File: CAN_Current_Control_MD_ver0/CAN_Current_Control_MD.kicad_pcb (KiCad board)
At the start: 2 copper layers, 75 x 81 mm, 200 parts, among them J1 SWD, J10 FAN, J11 OUT_0, J12 OUT_1, J13 VALVE, J2 CAN, J3 CAN, J4 ENC0, J5 ENC1, J6 I/O_0, J7 I/O_1, J8 BATT_IN, J9 BATT_IN, Q1 MOSFET_N, Q10 NPN, Q2 MOSFET_N, Q3 MOSFET_N, Q4 MOSFET_N, Q5 MOSFET_N, Q6 MOSFET_N, Q7 MOSFET_N, Q8 MOSFET_N, Q9 NPN, SW1 SW0, SW2 SW1, SW3 RST, U1 BD33FA1, U10 NCP5104, U11 NCP5104, U12 BD9G101G, U13 INA181A1, U14 INA181A1, U15 LOGO, U2 ISO1050DUB, U3 STM32F405RG, U4 ADRESS, U5 AZ1086H, U6 BD9G101G, U7 AQM0802, U8 NCP5104, U9 NCP5104, Y1 8MHz

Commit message: 電流制御MD(仮)配線(仮)完成(仮)
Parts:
- moved R31 0.39 mm to (186.5, 122.3)
- moved C14 0.28 mm to (188.3, 122.2)
- moved R30 0.25 mm to (191.2, 129.5)
- moved R32 0.25 mm to (189.8, 129.5)
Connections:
- U3 pad 20: /Substrate_Temp -> /ADRESS_1
- U3 pad 21: /ADRESS_4 -> /Substrate_Temp
- U3 pad 23: /ADRESS_1 -> /ADRESS_4
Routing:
- net GNDPWR: track 84.2 -> 164.3 mm, vias 93 -> 115
- net /ADRESS_1: track 0.00 -> 45.3 mm, vias 0 -> 4
- net /ADRESS_4: track 0.00 -> 38.4 mm, vias 0 -> 4
- net /ADRESS_8: track 0.00 -> 31.5 mm, vias 0 -> 6
- net /SWDIO: track 40.3 -> 45.4 mm
- net +5VP: track 113.0 -> 116.7 mm
- net /ADRESS_2: track 36.5 -> 38.6 mm
- net /SWCLK: track 41.3 -> 43.0 mm
- net Net-(C14-Pad1): track 3.17 -> 1.46 mm
- net /I2C2_SCL: track 10.7 -> 12.2 mm
- net /I2C2_SDA: track 8.92 -> 10.4 mm
- net /TIM3_CH2: track 39.1 -> 40.3 mm
- net /MD1R_Temp: track 49.1 -> 49.9 mm
- net /TIM3_CH1: track 41.5 -> 42.1 mm
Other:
- board text added: "12VP"
- board text added: "3V3"
- board text added: "CLK"
- board text added: "DIO"
- board text added: "Designed by A.Mizuta in 2020/03/01."
- board text added: "~RST"
- board text removed: "Designed by A.Mizuta in 2020/03/0."

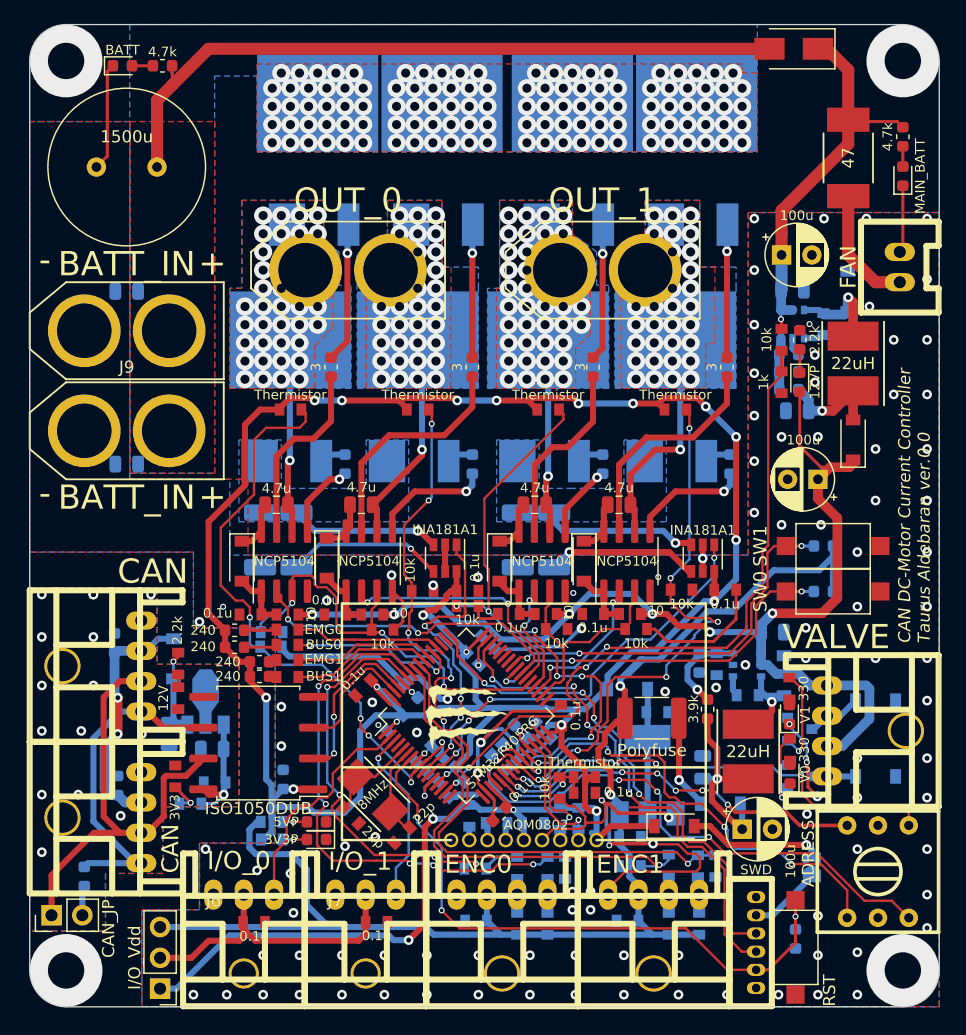
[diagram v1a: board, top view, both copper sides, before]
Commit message: 電流制御MDシリアル通信ポート忘れていたので，追加した
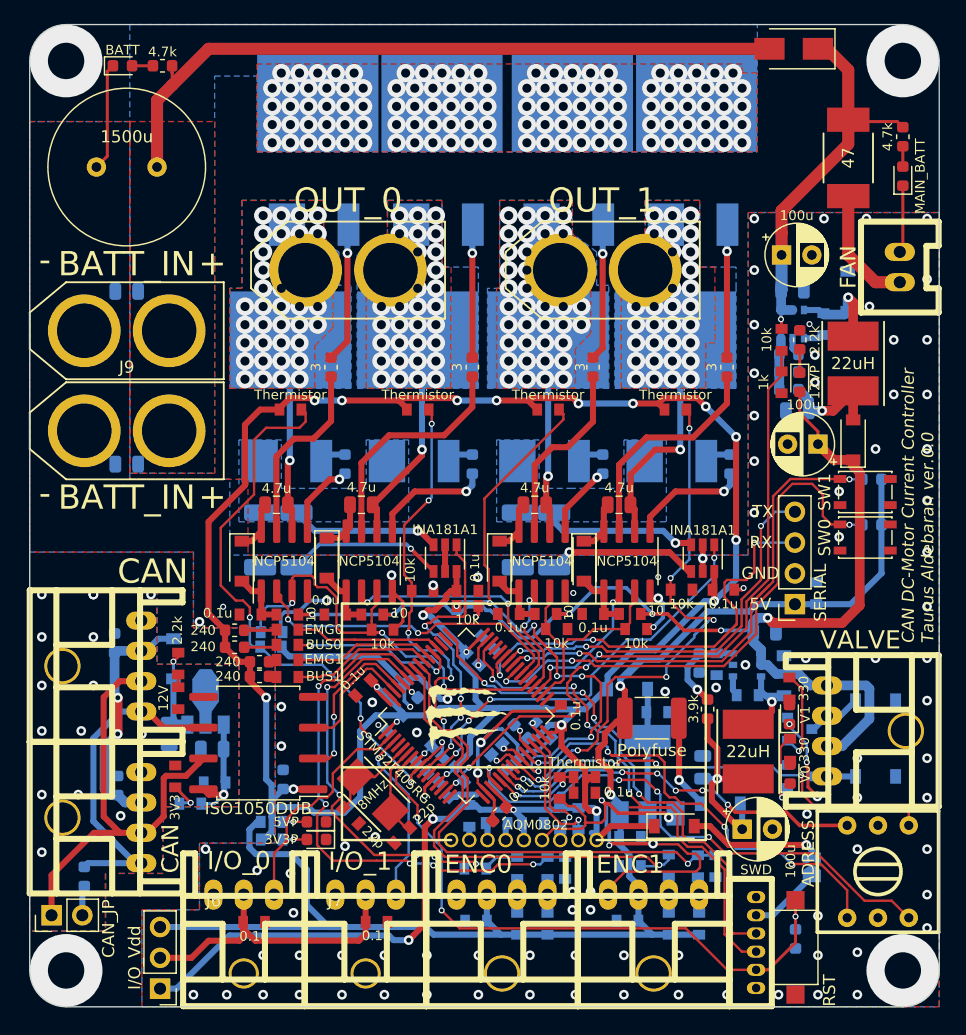
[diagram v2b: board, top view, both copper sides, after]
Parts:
- added C57: 0.1u, Mizz_lib:1608_WP, B.Cu at (210.9, 110.9)
- added J14: SERIAL, Connector_PinSocket_2.54mm:PinSocket_1x04_P2.54mm_Vertical, F.Cu at (209.1, 111.8)
- SW1, SW2: footprint Button_Switch_SMD:SW_SPST_CK_RS282G05A3 -> Button_Switch_SMD:SW_SPST_PTS810
- moved R10 6.80 mm to (215.4, 101.5)
- moved R8 6.80 mm to (215.4, 105.2)
- moved SW1 5.18 mm to (214.9, 106.3)
- moved SW2 5.18 mm to (214.9, 102.5)
- moved C50 2.90 mm to (211.0, 98.6)
- moved C25 0.65 mm to (206.6, 114.1)
- moved C56 0.15 mm to (203.2, 110.6)
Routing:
- net /USART1_RX: track 0.00 -> 38.4 mm, vias 0 -> 3
- net /USART1_TX: track 0.00 -> 33.0 mm, vias 0 -> 3
- net /SW0: track 31.2 -> 45.8 mm
- net /SW1: track 32.0 -> 43.4 mm
- net GNDPWR: track 164.3 -> 155.9 mm, vias 115 -> 113
- net +5VP: track 116.7 -> 124.0 mm
- net /MD1L_Temp: track 53.2 -> 56.0 mm
- net +12P: track 94.5 -> 96.9 mm
- net /MD1R_Temp: track 49.9 -> 51.2 mm
- net /EN0: track 36.8 -> 37.3 mm
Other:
- board text added: "5V"
- board text added: "H"
- board text added: "L"
- board text added: "RX"
- board text added: "TX"

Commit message: いろいろ修正しました
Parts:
- R50, R51, R52, R53, R54, R55, R56, R57: value 3 -> FILTER
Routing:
- net GNDPWR: track 155.9 -> 157.1 mm
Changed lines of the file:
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@@
     (thickness 1.6)
     (drawings 49)
-    (tracks 2194)
+    (tracks 2195)
     (zones 0)
     (modules 202)
@@
   )
   (setup
-    (last_trace_width 0.3)
+    (last_trace_width 0.25)
     (user_trace_width 0.2)
     (user_trace_width 0.3)
@@
       (effects (font (size 1 1) (thickness 0.15)))
     )
-    (fp_text value 3 (at 0 1.25 90) (layer F.SilkS)
+    (fp_text value FILTER (at 0 1.25 90) (layer F.SilkS)
       (effects (font (size 0.8 0.8) (thickness 0.15)))
     )
@@
       (effects (font (size 1 1) (thickness 0.15)) (justify mirror))
     )
-    (fp_text value 3 (at 0 -1.25 90) (layer B.SilkS)
+    (fp_text value FILTER (at 0 -1.25 90) (layer B.SilkS)
       (effects (font (size 0.8 0.8) (thickness 0.15)) (justify mirror))
     )
@@
       (effects (font (size 1 1) (thickness 0.15)))
     )
-    (fp_text value 3 (at 0 1.25 90) (layer F.SilkS)
+    (fp_text value FILTER (at 0 1.25 90) (layer F.SilkS)
       (effects (font (size 0.8 0.8) (thickness 0.15)))
     )
@@
       (effects (font (size 1 1) (thickness 0.15)) (justify mirror))
     )
-    (fp_text value 3 (at 0 -1.25 90) (layer B.SilkS)
+    (fp_text value FILTER (at 0 -1.25 90) (layer B.SilkS)
       (effects (font (size 0.8 0.8) (thickness 0.15)) (justify mirror))
     )
@@
       (effects (font (size 1 1) (thickness 0.15)))
     )
-    (fp_text value 3 (at 0 1.05 90) (layer F.SilkS)
+    (fp_text value FILTER (at 0 1.2 90) (layer F.SilkS)
       (effects (font (size 0.8 0.8) (thickness 0.15)))
     )
@@
       (effects (font (size 1 1) (thickness 0.15)) (justify mirror))
     )
-    (fp_text value 3 (at 0 -1.25 90) (layer B.SilkS)
+    (fp_text value FILTER (at 0 -1.25 90) (layer B.SilkS)
       (effects (font (size 0.8 0.8) (thickness 0.15)) (justify mirror))
     )
@@
       (effects (font (size 1 1) (thickness 0.15)))
     )
-    (fp_text value 3 (at 0 1.25 90) (layer F.SilkS)
+    (fp_text value FILTER (at 0 1.25 90) (layer F.SilkS)
       (effects (font (size 0.8 0.8) (thickness 0.15)))
     )
@@
       (effects (font (size 1 1) (thickness 0.15)) (justify mirror))
     )
-    (fp_text value 3 (at 0 -1.25 90) (layer B.SilkS)
+    (fp_text value FILTER (at 0 -1.25 90) (layer B.SilkS)
       (effects (font (size 0.8 0.8) (thickness 0.15)) (justify mirror))
     )
@@
   (via (at 160.5 132) (size 0.8) (drill 0.4) (layers F.Cu B.Cu) (net 5))
   (via (at 166.75 123.5) (size 0.8) (drill 0.4) (layers F.Cu B.Cu) (net 5))
-  (via (at 166.75 120.25) (size 0.8) (drill 0.4) (layers F.Cu B.Cu) (net 5))
   (via (at 160 113.25) (size 0.8) (drill 0.4) (layers F.Cu B.Cu) (net 5))
   (segment (start 208.9 90.7125) (end 209.3875 91.2) (width 0.5) (layer B.Cu) (net 5))
@@
   (segment (start 193.450001 129.509999) (end 193.450001 128.250001) (width 0.2) (layer F.Cu) (net 5))
   (segment (start 193.15 129.81) (end 193.450001 129.509999) (width 0.2) (layer F.Cu) (net 5))
-  (via (at 174.25 119.89) (size 0.8) (drill 0.4) (layers F.Cu B.Cu) (net 5))
   (via (at 174.75 121.76) (size 0.5) (drill 0.3) (layers F.Cu B.Cu) (net 5))
   (via (at 197.83 109.56) (size 0.5) (drill 0.3) (layers F.Cu B.Cu) (net 5))
@@
   (segment (start 183 111.95) (end 183 112.642501) (width 0.3) (layer F.Cu) (net 5))
   (segment (start 183 112.642501) (end 182.78 112.862501) (width 0.3) (layer F.Cu) (net 5))
+  (segment (start 169.5 117.5) (end 170.72217 117.5) (width 0.5) (layer B.Cu) (net 5))
+  (via (at 168.75 120.5) (size 0.8) (drill 0.4) (layers F.Cu B.Cu) (net 5))
+  (via (at 166.75 119) (size 0.8) (drill 0.4) (layers F.Cu B.Cu) (net 5))
   (segment (start 175.749569 127.435355) (end 175.75 127.434924) (width 0.2) (layer F.Cu) (net 6))
   (segment (start 175.749569 128.949569) (end 175.749569 127.435355) (width 0.2) (layer F.Cu) (net 6))
@@
   (segment (start 164.153882 112.06388) (end 164.153882 112.889669) (width 0.2) (layer F.Cu) (net 23))
   (segment (start 165.5 97.25) (end 164.5 98.25) (width 0.2) (layer F.Cu) (net 23))
-  (segment (start 165 115.3) (end 165.03 115.3) (width 0.2) (layer B.Cu) (net 23))
-  (segment (start 166.53 116.8) (end 170.124301 116.8) (width 0.2) (layer B.Cu) (net 23))
-  (segment (start 165.03 115.3) (end 166.53 116.8) (width 0.2) (layer B.Cu) (net 23))
   (via (at 173.290025 121.220025) (size 0.5) (drill 0.3) (layers F.Cu B.Cu) (net 23))
-  (segment (start 170.124301 116.8) (end 173.290025 119.965724) (width 0.2) (layer B.Cu) (net 23))
-  (segment (start 173.290025 119.965724) (end 173.290025 121.220025) (width 0.2) (layer B.Cu) (net 23))
   (via (at 173.95 122.63) (size 0.5) (drill 0.3) (layers F.Cu B.Cu) (net 23))
   (segment (start 173.290025 121.220025) (end 173.290025 121.970025) (width 0.2) (layer F.Cu) (net 23))
@@
   (segment (start 180.002438 123.389682) (end 180.072802 123.460046) (width 0.2) (layer B.Cu) (net 23))
   (segment (start 180.002438 123.177563) (end 180.002438 123.389682) (width 0.2) (layer B.Cu) (net 23))
+  (segment (start 165.03 115.3) (end 165 115.3) (width 0.2) (layer B.Cu) (net 23))
+  (segment (start 166.53 116.8) (end 165.03 115.3) (width 0.2) (layer B.Cu) (net 23))
+  (segment (start 170.8 116.8) (end 166.53 116.8) (width 0.2) (layer B.Cu) (net 23))
+  (segment (start 173.290025 121.220025) (end 173.290025 119.290025) (width 0.2) (layer B.Cu) (net 23))
+  (segment (start 173.290025 119.290025) (end 170.8 116.8) (width 0.2) (layer B.Cu) (net 23))
   (via (at 181.2 111.95) (size 0.5) (drill 0.3) (layers F.Cu B.Cu) (net 24))
   (segment (start 181.44 111.71) (end 181.2 111.95) (width 0.2) (layer B.Cu) (net 24))
@@
   (segment (start 184.5 132.65) (end 183.65 133.5) (width 0.25) (layer B.Cu) (net 93))
   (segment (start 186.2 132.65) (end 184.5 132.65) (width 0.25) (layer B.Cu) (net 93))
-  (via (at 170.536091 118.63) (size 0.5) (drill 0.3) (layers F.Cu B.Cu) (net 93))
   (segment (start 170.536091 124.350093) (end 170.54 124.354002) (width 0.2) (layer B.Cu) (net 93))
   (segment (start 170.536091 118.63) (end 170.536091 124.350093) (width 0.2) (layer B.Cu) (net 93))
@@
   (segment (start 183.26 133.21) (end 183.65 133.6) (width 0.2) (layer B.Cu) (net 93))
   (segment (start 182.79 133.21) (end 183.26 133.21) (width 0.2) (layer B.Cu) (net 93))
+  (via (at 170.536091 118.63) (size 0.5) (drill 0.3) (layers F.Cu B.Cu) (net 93))
   (segment (start 191.25 131.25) (end 191.25 130.4) (width 0.3) (layer B.Cu) (net 94))
   (segment (start 191.25 131.25) (end 191.25 130.077818) (width 0.2) (layer B.Cu) (net 94))

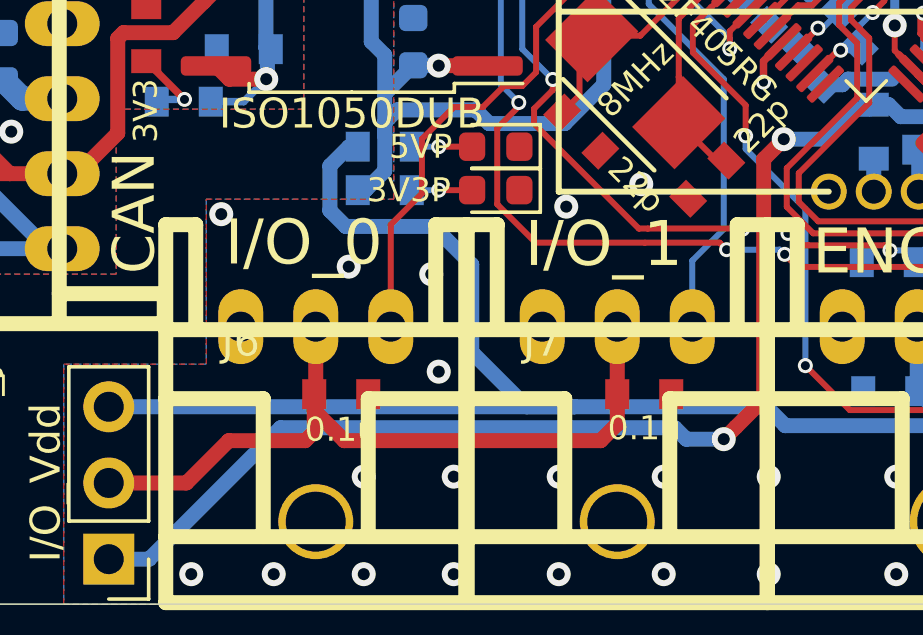
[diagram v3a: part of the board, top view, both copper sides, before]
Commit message: 電流制御用のMDのコンデンサの配置ミスがあったため，直した
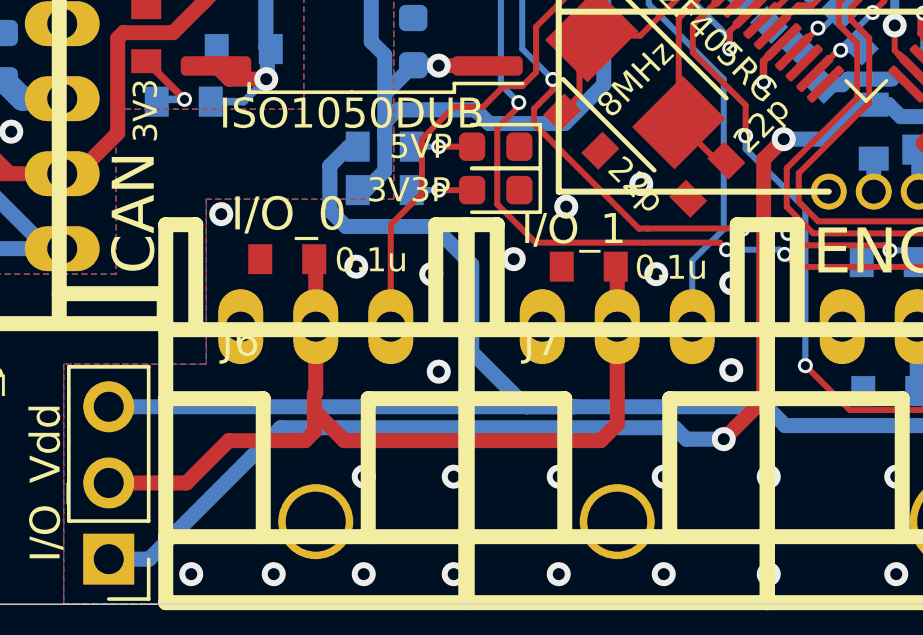
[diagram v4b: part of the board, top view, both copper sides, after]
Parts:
- moved C23 4.85 mm to (162.7, 133.5), turned to 0 degrees
- moved C24 4.64 mm to (172.8, 133.8), turned to 0 degrees
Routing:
- net Net-(C23-Pad2): track 25.1 -> 29.4 mm
- net GNDPWR: vias 113 -> 117
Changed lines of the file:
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@@
-(kicad_pcb (version 20171130) (host pcbnew "(5.1.4)-1")
+(kicad_pcb (version 20171130) (host pcbnew "(5.1.5)-3")
   (general
     (thickness 1.6)
     (drawings 49)
-    (tracks 2195)
+    (tracks 2203)
     (zones 0)
     (modules 202)
@@
   )
   (setup
-    (last_trace_width 0.25)
+    (last_trace_width 0.2)
     (user_trace_width 0.2)
     (user_trace_width 0.3)
@@
       (effects (font (size 1 1) (thickness 0.15)))
     )
-    (fp_text value I/O_0 (at 2.1 -2.8) (layer F.SilkS)
-      (effects (font (size 1.5 1.5) (thickness 0.3)))
+    (fp_text value I/O_0 (at 1.6 -3.75) (layer F.SilkS)
+      (effects (font (size 1.1 1.1) (thickness 0.275)))
     )
     (fp_line (start 6.5 -3.4) (end 6.5 0.1) (layer F.SilkS) (width 0.5))
@@
       (effects (font (size 1 1) (thickness 0.15)))
     )
-    (fp_text value I/O_1 (at 2.05 -2.75) (layer F.SilkS)
-      (effects (font (size 1.5 1.5) (thickness 0.3)))
+    (fp_text value I/O_1 (at 1.05 -3.25) (layer F.SilkS)
+      (effects (font (size 1 1) (thickness 0.25)))
     )
     (fp_line (start -2.5 -3.4) (end -2.5 9.2) (layer F.SilkS) (width 0.5))
@@
   )
   (module Mizz_lib:1608_WP (layer F.Cu)
-    (at 164.5 138 180)
+    (at 162.7 133.5)
     (descr <b>CAPACITOR</b>)
     (fp_text reference C23 (at -0.635 -0.635) (layer F.SilkS) hide
-      (effects (font (size 1.2065 1.2065) (thickness 0.1016)) (justify right bottom))
+      (effects (font (size 1.2065 1.2065) (thickness 0.1016)) (justify left bottom))
     )
-    (fp_text value 0.1u (at 0 -1.65) (layer F.SilkS)
+    (fp_text value 0.1u (at 2.8 0.5) (layer F.SilkS)
       (effects (font (size 0.8 0.8) (thickness 0.15)) (justify bottom))
     )
@@
     (fp_poly (pts (xy 0.3302 0.4699) (xy 0.8303 0.4699) (xy 0.8303 -0.4801) (xy 0.3302 -0.4801)) (layer Dwgs.User) (width 0))
     (fp_poly (pts (xy -0.1999 0.3) (xy 0.1999 0.3) (xy 0.1999 -0.3) (xy -0.1999 -0.3)) (layer F.Adhes) (width 0))
-    (pad 1 smd rect (at -0.9 0 180) (size 0.8 1) (layers F.Cu F.Paste F.Mask)
+    (pad 1 smd rect (at -0.9 0) (size 0.8 1) (layers F.Cu F.Paste F.Mask)
       (net 5 GNDPWR))
-    (pad 2 smd rect (at 0.9 0 180) (size 0.8 1) (layers F.Cu F.Paste F.Mask)
+    (pad 2 smd rect (at 0.9 0) (size 0.8 1) (layers F.Cu F.Paste F.Mask)
       (net 16 "Net-(C23-Pad2)"))
     (model ${KISYS3DMOD}/Resistor_SMD.3dshapes/R_0603_1608Metric.step
@@
   )
   (module Mizz_lib:1608_WP (layer F.Cu)
-    (at 174.6 138 180)
+    (at 172.75 133.75)
     (descr <b>CAPACITOR</b>)
     (fp_text reference C24 (at -0.635 -0.635) (layer F.SilkS) hide
-      (effects (font (size 1.2065 1.2065) (thickness 0.1016)) (justify right bottom))
+      (effects (font (size 1.2065 1.2065) (thickness 0.1016)) (justify left bottom))
     )
-    (fp_text value 0.1u (at 0 -1.6) (layer F.SilkS)
+    (fp_text value 0.1u (at 2.75 0.5) (layer F.SilkS)
       (effects (font (size 0.8 0.8) (thickness 0.15)) (justify bottom))
     )
@@
     (fp_line (start -0.356 0.419) (end 0.356 0.419) (layer Dwgs.User) (width 0.1016))
     (fp_line (start -0.356 -0.432) (end 0.356 -0.432) (layer Dwgs.User) (width 0.1016))
-    (pad 2 smd rect (at 0.9 0 180) (size 0.8 1) (layers F.Cu F.Paste F.Mask)
+    (pad 2 smd rect (at 0.9 0) (size 0.8 1) (layers F.Cu F.Paste F.Mask)
       (net 16 "Net-(C23-Pad2)"))
-    (pad 1 smd rect (at -0.9 0 180) (size 0.8 1) (layers F.Cu F.Paste F.Mask)
+    (pad 1 smd rect (at -0.9 0) (size 0.8 1) (layers F.Cu F.Paste F.Mask)
       (net 5 GNDPWR))
     (model ${KISYS3DMOD}/Resistor_SMD.3dshapes/R_0603_1608Metric.step
@@
   (via (at 167.5 134) (size 0.8) (drill 0.4) (layers F.Cu B.Cu) (net 5))
   (via (at 167.75 137.25) (size 0.8) (drill 0.4) (layers F.Cu B.Cu) (net 5))
-  (via (at 164.75 133.75) (size 0.8) (drill 0.4) (layers F.Cu B.Cu) (net 5))
   (via (at 170.5 111.5) (size 0.8) (drill 0.4) (layers F.Cu B.Cu) (net 5))
   (via (at 182.96 109.58) (size 0.8) (drill 0.4) (layers F.Cu B.Cu) (net 5))
@@
   (via (at 168.75 120.5) (size 0.8) (drill 0.4) (layers F.Cu B.Cu) (net 5))
   (via (at 166.75 119) (size 0.8) (drill 0.4) (layers F.Cu B.Cu) (net 5))
+  (via (at 165 133.75) (size 0.8) (drill 0.4) (layers F.Cu B.Cu) (net 5))
+  (via (at 170.25 133.5) (size 0.8) (drill 0.4) (layers F.Cu B.Cu) (net 5))
+  (via (at 177.5 137.2) (size 0.8) (drill 0.4) (layers F.Cu B.Cu) (net 5))
+  (via (at 177.5 134.3) (size 0.8) (drill 0.4) (layers F.Cu B.Cu) (net 5))
+  (via (at 175 134) (size 0.8) (drill 0.4) (layers F.Cu B.Cu) (net 5))
   (segment (start 175.749569 127.435355) (end 175.75 127.434924) (width 0.2) (layer F.Cu) (net 6))
   (segment (start 175.749569 128.949569) (end 175.749569 127.435355) (width 0.2) (layer F.Cu) (net 6))
@@
   (segment (start 159.34 140.96) (end 156.75 140.96) (width 0.5) (layer F.Cu) (net 16))
   (segment (start 160.75 139.55) (end 159.34 140.96) (width 0.5) (layer F.Cu) (net 16))
+  (segment (start 163.65 133.55) (end 163.6 133.5) (width 0.5) (layer F.Cu) (net 16))
+  (segment (start 163.65 135.75) (end 163.65 133.55) (width 0.5) (layer F.Cu) (net 16))
+  (segment (start 173.7 133.8) (end 173.65 133.75) (width 0.5) (layer F.Cu) (net 16))
+  (segment (start 173.7 135.75) (end 173.7 133.8) (width 0.5) (layer F.Cu) (net 16))
   (segment (start 206.3125 115.8475) (end 206.31 115.85) (width 0.8) (layer B.Cu) (net 17))
   (segment (start 206.31 115.85) (end 206.31 116.8) (width 0.8) (layer B.Cu) (net 17))
